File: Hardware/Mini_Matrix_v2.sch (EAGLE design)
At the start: 40 parts, among them U2 MCP73831, U3 MIC5219-3.3

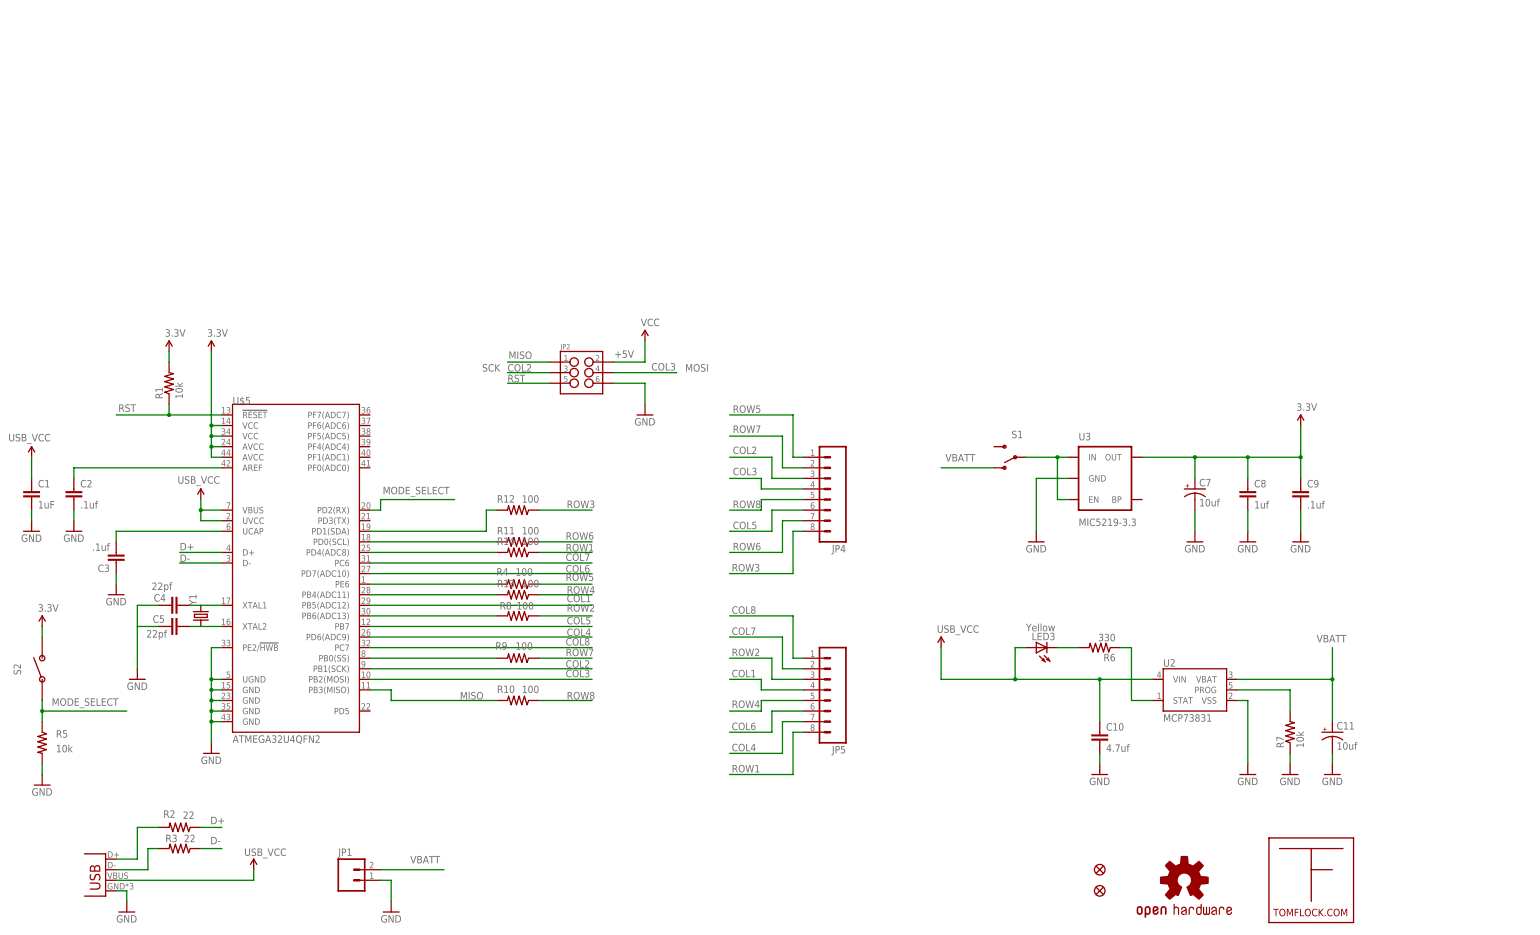
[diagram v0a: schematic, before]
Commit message: Added detailed Documentation
Assembly Drawing
Schematic
Stencil
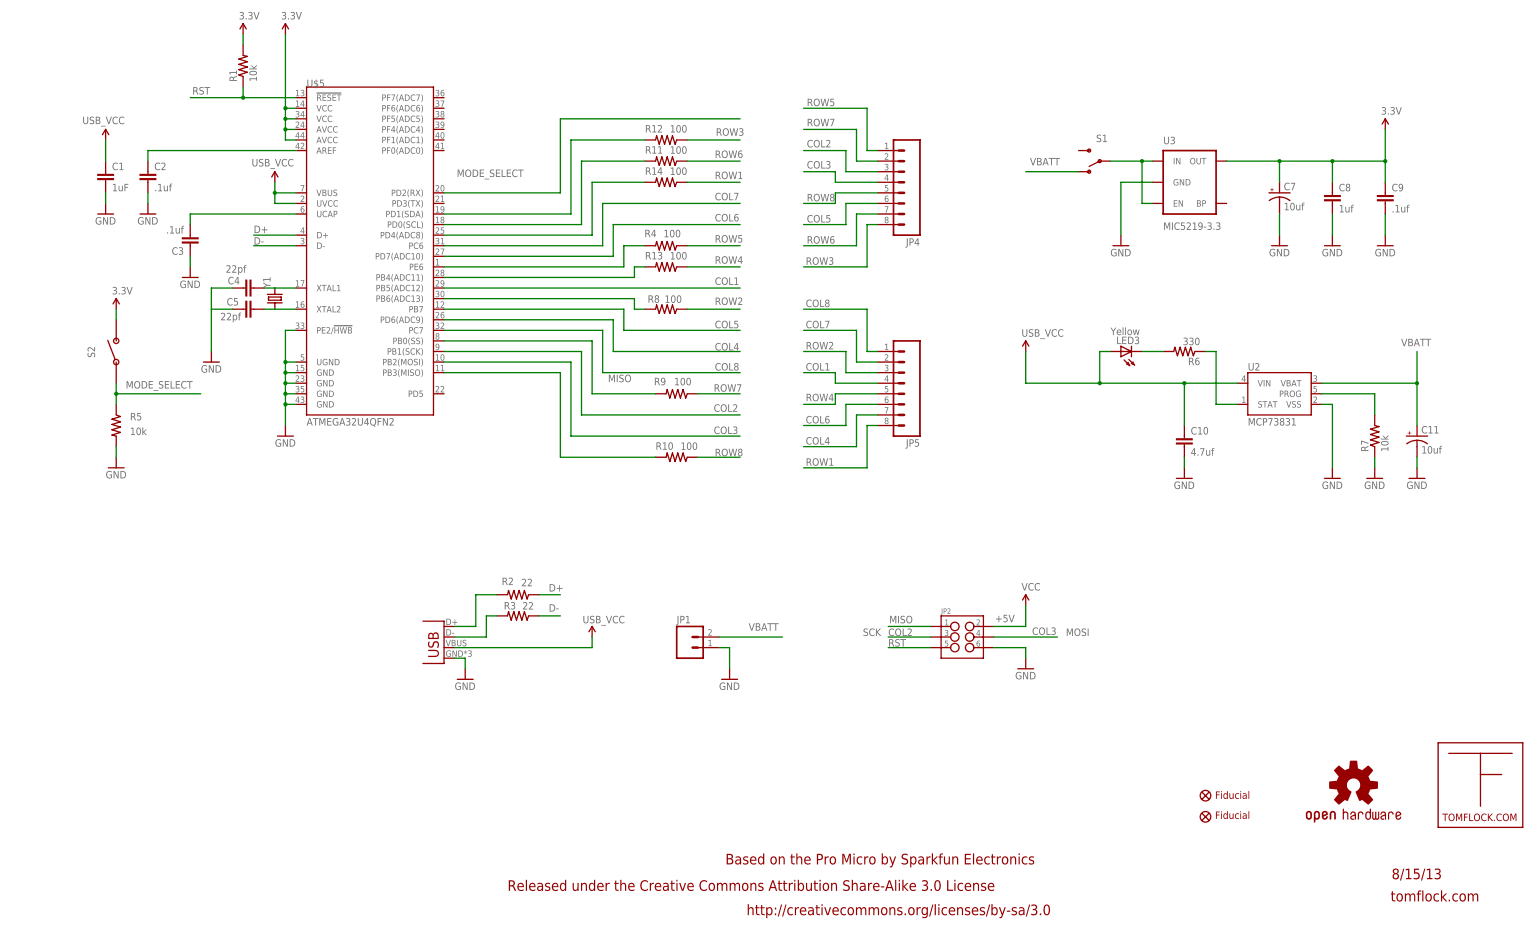
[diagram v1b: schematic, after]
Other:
- note added: "8/15/13"
- note added: "Based on the Pro Micro by Sparkfun Electronics"
- note added: "Fiducial"
- note added: "Released under the Creative Commons Attribution Share-Alike 3.0 License"
- note added: "http://creativecommons.org/licenses/by-sa/3.0"
- note added: "tomflock.com"
- moved on the sheet: C1, C10, C11, C2, C3, C4, C5, C7, C8, C9, JP1, JP2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
